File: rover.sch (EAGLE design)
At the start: 14 parts, among them IC1 MC33269ST-5.0T3, J1 B02B-PASK(LF)(SN)

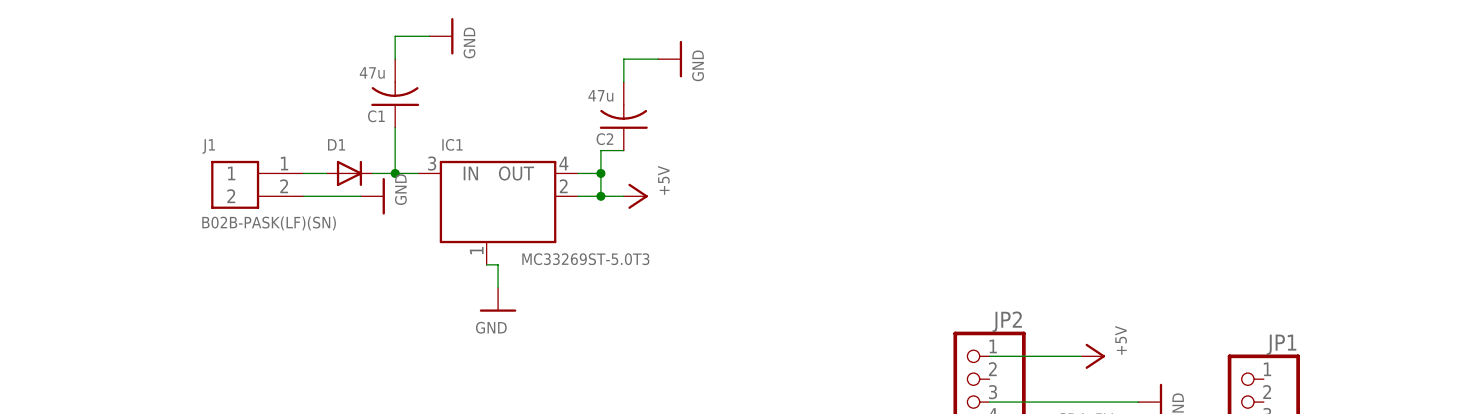
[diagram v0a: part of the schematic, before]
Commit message: added led and power switch
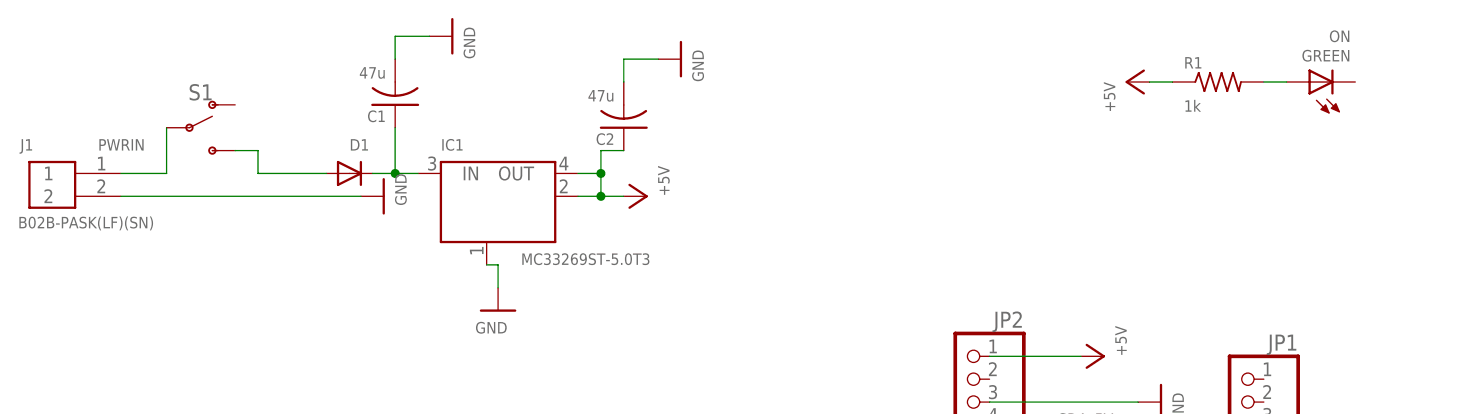
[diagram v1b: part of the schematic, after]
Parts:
- added GREEN: ON, adafruit:LEDCHIP-LED0805
- added R1: 1k, adafruit:R-US_R0603
- added S1: (no value), SparkFun-Switches:SWITCH-SPDT-SMD-AYZ0202
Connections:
- new net N$3: D1.A, S1.S
- new net PWRIN: J1.1, S1.P
- net +5V: now also R1.1
- net N$1: now also GREEN.A, R1.2; no longer D1.A, J1.1
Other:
- moved on the sheet: J1
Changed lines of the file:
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@@
 <part name="C2" library="adafruit" library_urn="urn:adsk.eagle:library:420" deviceset="C-US" device="C1206" package3d_urn="urn:adsk.eagle:package:6240335/1" value="47u"/>
 <part name="GND12" library="SparkFun" deviceset="GND" device=""/>
+<part name="S1" library="SparkFun-Switches" library_urn="urn:adsk.eagle:library:535" deviceset="SWITCH-SPDT" device="-SMD-AYZ0202" package3d_urn="urn:adsk.eagle:package:40160/1"/>
+<part name="GREEN" library="adafruit" library_urn="urn:adsk.eagle:library:420" deviceset="LED" device="CHIP-LED0805" package3d_urn="urn:adsk.eagle:package:6240557/1" value="ON"/>
+<part name="P+9" library="supply1" library_urn="urn:adsk.eagle:library:371" deviceset="+5V" device=""/>
+<part name="R1" library="adafruit" library_urn="urn:adsk.eagle:library:420" deviceset="R-US_" device="R0603" package3d_urn="urn:adsk.eagle:package:6240565/1" value="1k"/>
 </parts>
 <sheets>
@@
 <attribute name="VALUE" x="58.42" y="55.88" size="1.27" layer="96" rot="R270"/>
 </instance>
-<instance part="J1" gate="G$1" x="-53.34" y="106.68" smashed="yes">
-<attribute name="NAME" x="-56.896" y="111.76" size="1.27" layer="95"/>
-<attribute name="VALUE" x="-57.15" y="103.124" size="1.27" layer="96"/>
+<instance part="J1" gate="G$1" x="-73.66" y="106.68" smashed="yes">
+<attribute name="NAME" x="-77.216" y="111.76" size="1.27" layer="95"/>
+<attribute name="VALUE" x="-77.47" y="103.124" size="1.27" layer="96"/>
 </instance>
 <instance part="P+2" gate="1" x="-7.62" y="106.68" smashed="yes" rot="R270">
@@
 </instance>
 <instance part="D1" gate="G$1" x="-40.64" y="109.22" smashed="yes">
-<attribute name="NAME" x="-43.18" y="111.76" size="1.27" layer="95"/>
+<attribute name="NAME" x="-40.64" y="111.76" size="1.27" layer="95"/>
 <attribute name="VALUE" x="-43.18" y="105.41" size="1.27" layer="96"/>
 </instance>
@@
 <instance part="GND12" gate="1" x="-3.81" y="121.92" smashed="yes" rot="R90">
 <attribute name="VALUE" x="-1.27" y="119.38" size="1.27" layer="96" rot="R90"/>
+</instance>
+<instance part="S1" gate="1" x="-58.42" y="114.3" smashed="yes">
+<attribute name="NAME" x="-57.15" y="117.348" size="1.778" layer="95" font="vector" align="bottom-center"/>
+<attribute name="VALUE" x="-57.404" y="110.998" size="1.778" layer="96" font="vector" align="top-center"/>
+</instance>
+<instance part="GREEN" gate="G$1" x="66.04" y="119.38" smashed="yes" rot="R90">
+<attribute name="NAME" x="70.612" y="122.936" size="1.27" layer="95" rot="R180"/>
+<attribute name="VALUE" x="70.612" y="125.095" size="1.27" layer="96" rot="R180"/>
+</instance>
+<instance part="P+9" gate="1" x="45.72" y="119.38" smashed="yes" rot="R90">
+<attribute name="VALUE" x="43.18" y="119.38" size="1.27" layer="96" rot="R270"/>
+</instance>
+<instance part="R1" gate="G$1" x="55.88" y="119.38" smashed="yes">
+<attribute name="NAME" x="52.07" y="120.8786" size="1.27" layer="95"/>
+<attribute name="VALUE" x="52.07" y="116.078" size="1.27" layer="96"/>
 </instance>
 </instances>
@@
 <pinref part="J1" gate="G$1" pin="2"/>
 <pinref part="GND10" gate="1" pin="GND"/>
-<wire x1="-45.72" y1="106.68" x2="-39.37" y2="106.68" width="0.1524" layer="91"/>
+<wire x1="-66.04" y1="106.68" x2="-39.37" y2="106.68" width="0.1524" layer="91"/>
 </segment>
 <segment>
@@
 <junction x="-12.7" y="109.22"/>
 </segment>
-</net>
-<net name="N$1" class="0">
-<segment>
-<pinref part="J1" gate="G$1" pin="1"/>
-<pinref part="D1" gate="G$1" pin="A"/>
-<wire x1="-45.72" y1="109.22" x2="-43.18" y2="109.22" width="0.1524" layer="91"/>
+<segment>
+<pinref part="P+9" gate="1" pin="+5V"/>
+<pinref part="R1" gate="G$1" pin="1"/>
+<wire x1="48.26" y1="119.38" x2="50.8" y2="119.38" width="0.1524" layer="91"/>
 </segment>
 </net>
@@
 </segment>
 </net>
+<net name="PWRIN" class="0">
+<segment>
+<pinref part="J1" gate="G$1" pin="1"/>
+<pinref part="S1" gate="1" pin="P"/>
+<wire x1="-66.04" y1="109.22" x2="-60.96" y2="109.22" width="0.1524" layer="91"/>
+<wire x1="-60.96" y1="109.22" x2="-60.96" y2="114.3" width="0.1524" layer="91"/>
+<label x="-68.58" y="111.76" size="1.27" layer="95"/>
+</segment>
+</net>
+<net name="N$3" class="0">
+<segment>
+<pinref part="S1" gate="1" pin="S"/>
+<wire x1="-53.34" y1="111.76" x2="-50.8" y2="111.76" width="0.1524" layer="91"/>
+<wire x1="-50.8" y1="111.76" x2="-50.8" y2="109.22" width="0.1524" layer="91"/>
+<pinref part="D1" gate="G$1" pin="A"/>
+<wire x1="-50.8" y1="109.22" x2="-43.18" y2="109.22" width="0.1524" layer="91"/>
+</segment>
+</net>
+<net name="N$1" class="0">
+<segment>
+<pinref part="R1" gate="G$1" pin="2"/>
+<pinref part="GREEN" gate="G$1" pin="A"/>
+<wire x1="60.96" y1="119.38" x2="63.5" y2="119.38" width="0.1524" layer="91"/>
+</segment>
+</net>
